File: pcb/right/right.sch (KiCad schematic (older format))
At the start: 103 parts, among them SW1 SW_Push, SW10 SW_Push, SW11 SW_Push, SW12 SW_Push, SW13 SW_Push, SW14 SW_Push, SW15 SW_Push, SW16 SW_Push, SW17 SW_Push, SW18 SW_Push, SW19 SW_Push, SW2 SW_Push, SW20 SW_Push, SW21 SW_Push, SW22 SW_Push, SW23 SW_Push, SW24 SW_Push, SW25 SW_Push, SW26 SW_Push, SW27 SW_Push, SW28 SW_Push, SW29 SW_Push, SW3 SW_Push, SW30 SW_Push, SW31 SW_Push, SW32 SW_Push, SW33 SW_Push, SW34 SW_Push, SW35 SW_Push, SW36 SW_Push, SW37 SW_Push, SW38 SW_Push, SW39 SW_Push, SW4 SW_Push, SW40 SW_Push, SW41 SW_Push, SW42 SW_Push, SW43 SW_Push, SW44 SW_Push, SW45 SW_Push, SW46 SW_Push, SW47 SW_Push, SW48 SW_Push, SW49 SW_Push, SW5 SW_Push, SW50 SW_Push, SW51 SW_Push, SW52 SW_Push, SW6 SW_Push, SW7 SW_Push, SW8 SW_Push, SW9 SW_Push

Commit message: pcb: Right key layout
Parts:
- SW43: footprint Button_Switch_Keyboard:SW_Cherry_MX_1.00u_PCB -> Button_Switch_Keyboard:SW_Cherry_MX_1.50u_PCB
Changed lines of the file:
@@
 F 0 "SW43" H 9950 2635 50  0000 C CNN
 F 1 "SW_Push" H 9950 2544 50  0000 C CNN
-F 2 "Button_Switch_Keyboard:SW_Cherry_MX_1.00u_PCB" H 9950 2550 50  0001 C CNN
+F 2 "Button_Switch_Keyboard:SW_Cherry_MX_1.50u_PCB" H 9950 2550 50  0001 C CNN
 F 3 "~" H 9950 2550 50  0001 C CNN
 	1    9950 2350

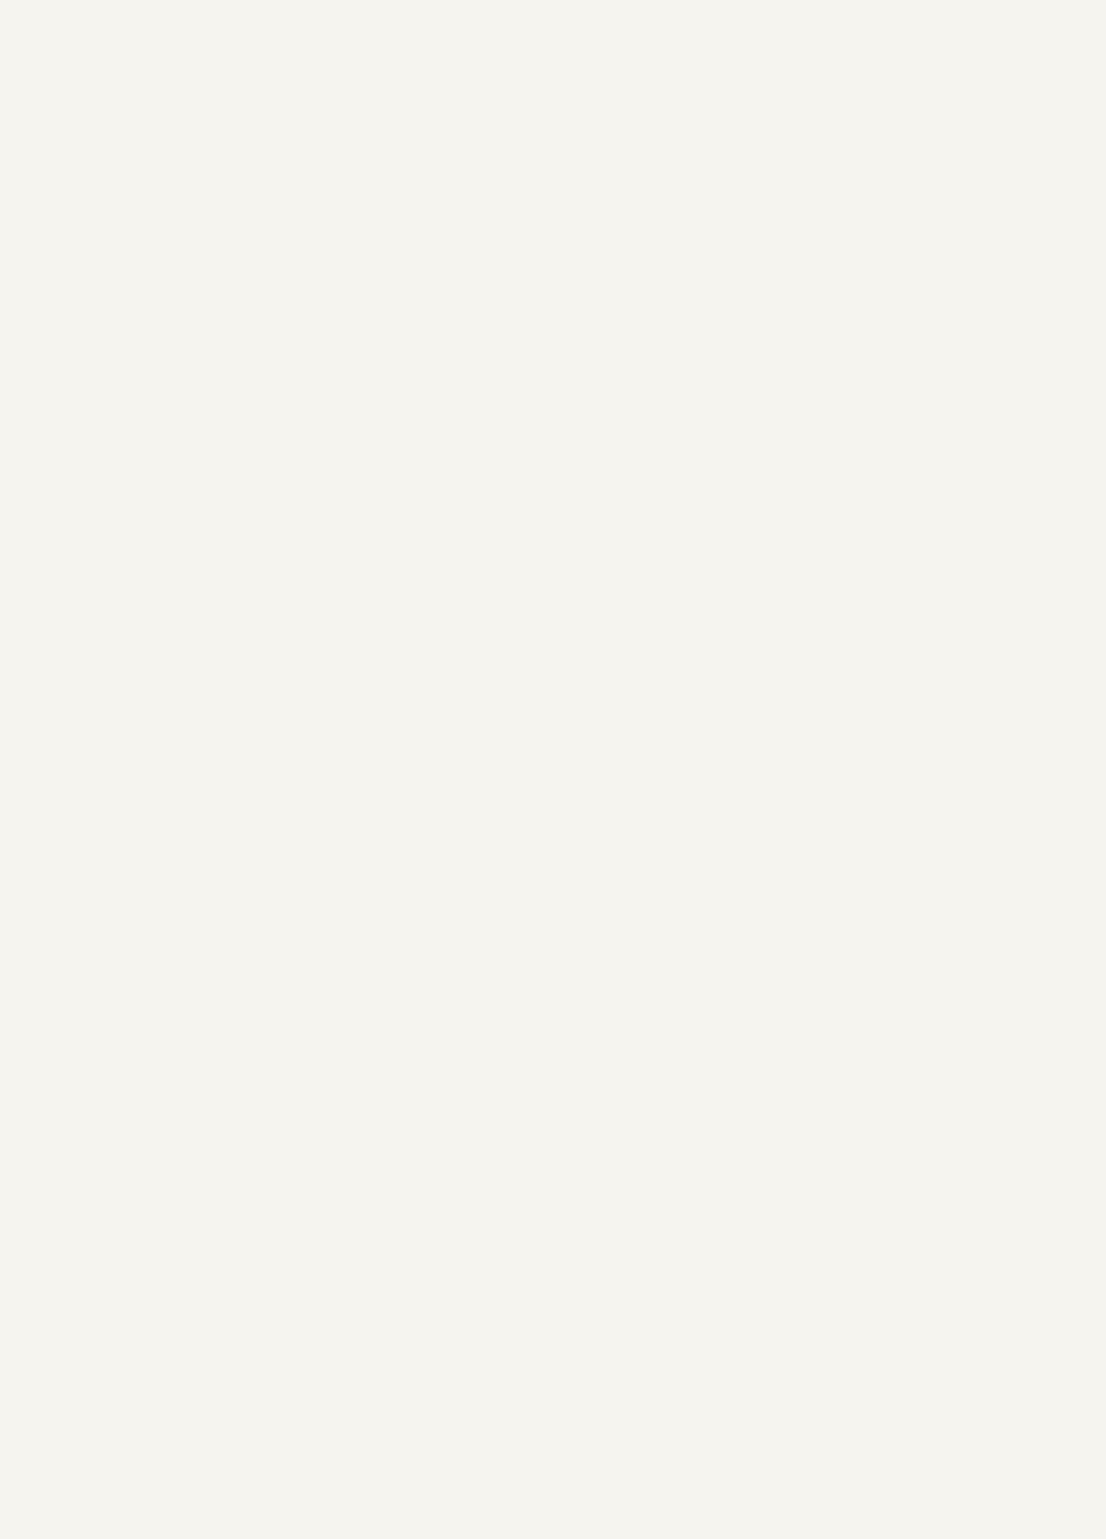
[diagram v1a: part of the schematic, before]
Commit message: pcb: right: Power to MCU
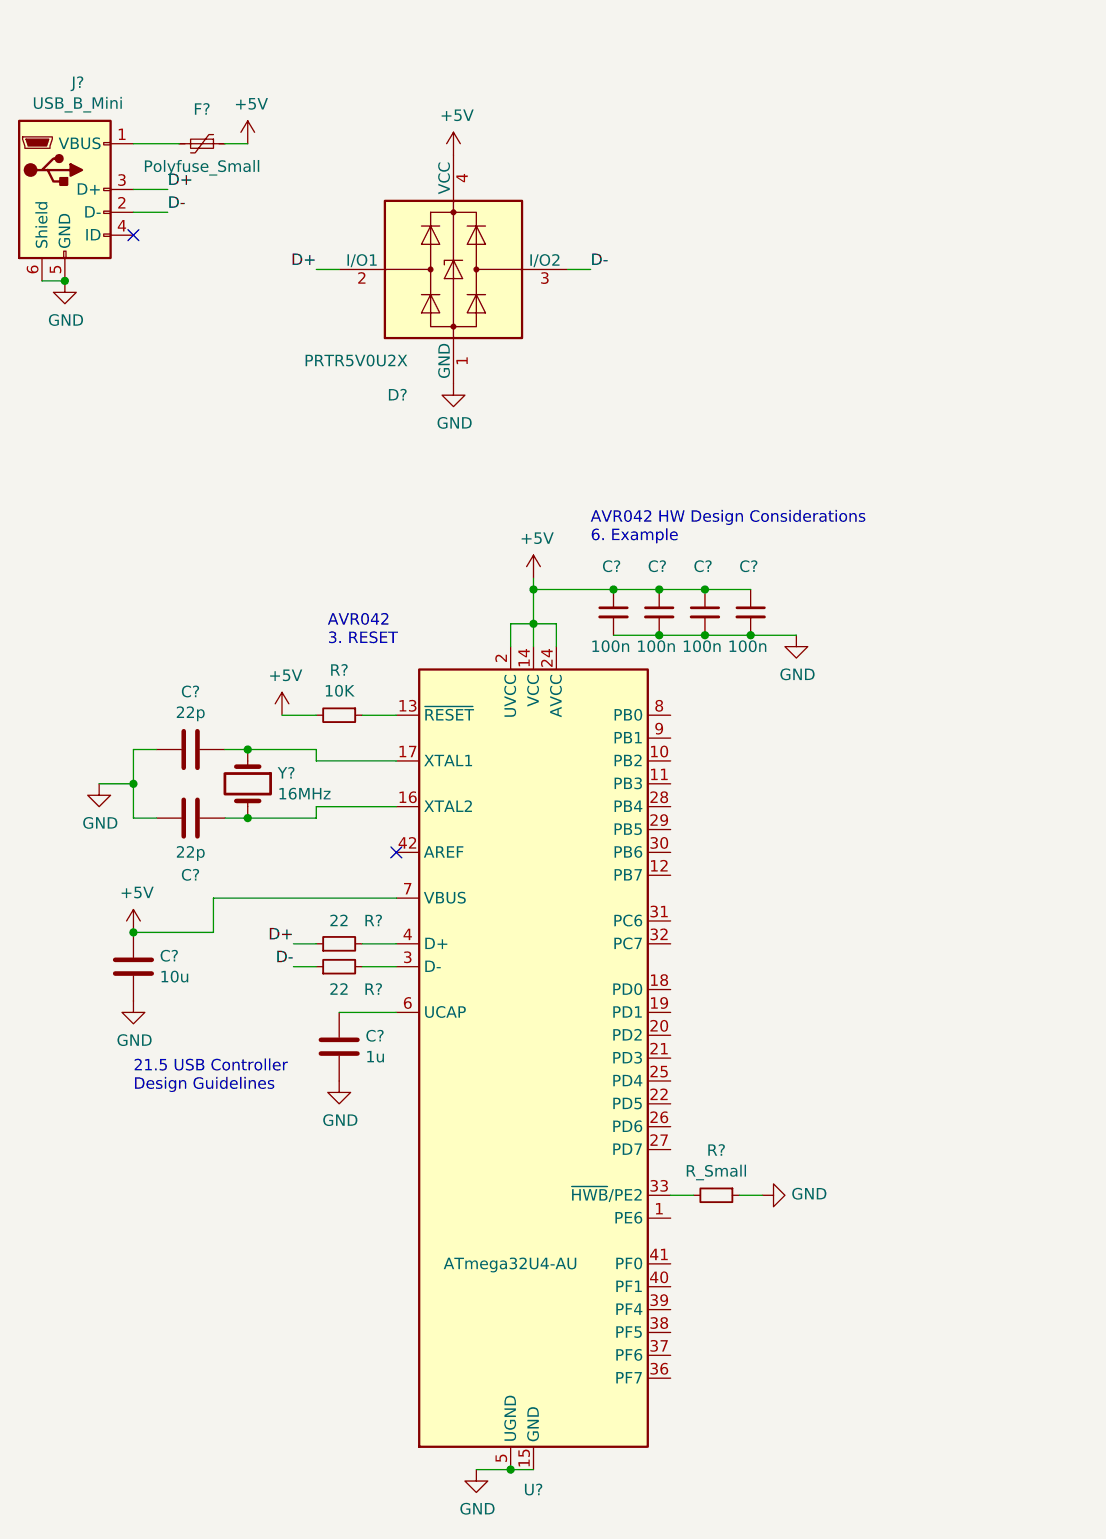
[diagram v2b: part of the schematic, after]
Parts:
- added C?: 1u, symbol Device:C
- added C? (x2): 22p, symbol Device:C
- added C?: 10u, symbol Device:C
- added C? (x4): 100n, symbol Device:C_Small
- added D?: PRTR5V0U2X, Package_TO_SOT_SMD:SOT-143, symbol Power_Protection:PRTR5V0U2X
- added F?: Polyfuse_Small, symbol Device:Polyfuse_Small
- added J?: USB_B_Mini, symbol Connector:USB_B_Mini
- added R?: R_Small, symbol Device:R_Small
- added R? (x2): 22, symbol Device:R_Small
- added R?: 10K, symbol Device:R_Small
- added U?: ATmega32U4-AU, Package_QFP:TQFP-44_10x10mm_P0.8mm, symbol MCU_Microchip_ATmega:ATmega32U4-AU
- added Y?: 16MHz, symbol Device:Crystal
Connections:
- net labels added: +5V, D+, D-, GND
- wire segments 120 -> 169
- no-connect marks 0 -> 2
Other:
- note added: "21.5 USB Controller\nDesign Guidelines"
- note added: "AVR042 HW Design Considerations\n6. Example"
- note added: "AVR042\n3. RESET"

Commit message: pcb: Right: Reset
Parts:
- added D?: D_Small, symbol Device:D_Small
- added SW?: SW_Push, symbol Switch:SW_Push
- R?: value R_Small -> 10K
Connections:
- wire segments 169 -> 175
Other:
- note added: "AVR042\n3. RESET\n+ Arduino"
- note removed: "AVR042\n3. RESET"
- moved on the sheet: R?
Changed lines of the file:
@@
 L power:+5V #PWR?
 U 1 1 604E6BA1
-P 1750 3700
-F 0 "#PWR?" H 1750 3550 50  0001 C CNN
-F 1 "+5V" H 1765 3873 50  0000 C CNN
-F 2 "" H 1750 3700 50  0001 C CNN
-F 3 "" H 1750 3700 50  0001 C CNN
-	1    1750 3700
+P 2150 3150
+F 0 "#PWR?" H 2150 3000 50  0001 C CNN
+F 1 "+5V" H 2165 3323 50  0000 C CNN
+F 2 "" H 2150 3150 50  0001 C CNN
+F 3 "" H 2150 3150 50  0001 C CNN
+	1    2150 3150
 	1    0    0    -1
 $EndComp
@@
 L Device:R_Small R?
 U 1 1 605D1F9D
-P 2000 3700
-F 0 "R?" V 1804 3700 50  0000 C CNN
-F 1 "10K" V 1895 3700 50  0000 C CNN
-F 2 "" H 2000 3700 50  0001 C CNN
-F 3 "~" H 2000 3700 50  0001 C CNN
-	1    2000 3700
-	0    1    1    0
-$EndComp
-Wire Wire Line
-	2100 3700 2250 3700
-Wire Wire Line
-	1900 3700 1750 3700
+P 2150 3300
+F 0 "R?" H 2050 3250 50  0000 C CNN
+F 1 "10K" H 2050 3350 50  0000 C CNN
+F 2 "" H 2150 3300 50  0001 C CNN
+F 3 "~" H 2150 3300 50  0001 C CNN
+	1    2150 3300
+	-1   0    0    1
+$EndComp
 $Comp
 L Device:C C?
@@
 Text Notes 3100 2950 0    50   ~ 0
 AVR042 HW Design Considerations\n6. Example
-Text Notes 1950 3400 0    50   ~ 0
-AVR042\n3. RESET
+Text Notes 1650 3100 0    50   ~ 0
+AVR042\n3. RESET\n+ Arduino
 $Comp
 L power:GND #PWR?
@@
 P 3650 5800
 F 0 "R?" V 3454 5800 50  0000 C CNN
-F 1 "R_Small" V 3545 5800 50  0000 C CNN
+F 1 "10K" V 3545 5800 50  0000 C CNN
 F 2 "" H 3650 5800 50  0001 C CNN
 F 3 "~" H 3650 5800 50  0001 C CNN
@@
 Wire Wire Line
 	3750 5800 3850 5800
+$Comp
+L Switch:SW_Push SW?
+U 1 1 60403708
+P 1900 3500
+F 0 "SW?" H 1900 3785 50  0000 C CNN
+F 1 "SW_Push" H 1900 3694 50  0000 C CNN
+F 2 "" H 1900 3700 50  0001 C CNN
+F 3 "~" H 1900 3700 50  0001 C CNN
+	1    1900 3500
+	1    0    0    -1
+$EndComp
+$Comp
+L power:GND #PWR?
+U 1 1 6040463B
+P 1600 3500
+F 0 "#PWR?" H 1600 3250 50  0001 C CNN
+F 1 "GND" H 1605 3327 50  0000 C CNN
+F 2 "" H 1600 3500 50  0001 C CNN
+F 3 "" H 1600 3500 50  0001 C CNN
+	1    1600 3500
+	1    0    0    -1
+$EndComp
+Wire Wire Line
+	1700 3500 1600 3500
+Wire Wire Line
+	2150 3150 2150 3200
+Wire Wire Line
+	2100 3500 2150 3500
+Wire Wire Line
+	2150 3500 2150 3700
+Wire Wire Line
+	2150 3700 2250 3700
+Wire Wire Line
+	2150 3400 2150 3500
+Connection ~ 2150 3500
+$Comp
+L Device:D_Small D?
+U 1 1 604C1548
+P 2400 3300
+F 0 "D?" V 2400 3370 50  0000 L CNN
+F 1 "D_Small" V 2445 3370 50  0001 L CNN
+F 2 "" V 2400 3300 50  0001 C CNN
+F 3 "~" V 2400 3300 50  0001 C CNN
+	1    2400 3300
+	0    1    1    0
+$EndComp
+Wire Wire Line
+	2400 3400 2150 3400
+Connection ~ 2150 3400
+Wire Wire Line
+	2400 3200 2150 3200
+Connection ~ 2150 3200
 $EndSCHEMATC

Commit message: pcb: right: ICSP, I2C
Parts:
- added C?: 100n, symbol Device:C_Small
- added J?: ICSP, symbol Connector_Generic:Conn_02x03_Odd_Even
- added J?: To Left Part, symbol Connector_Generic:Conn_02x02_Odd_Even
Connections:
- net labels added: MISO, MOSI, RESET, SCK, SCL, SDA
- wire segments 175 -> 192
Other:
- moved on the sheet: D?, F?, J?, R?, SW?

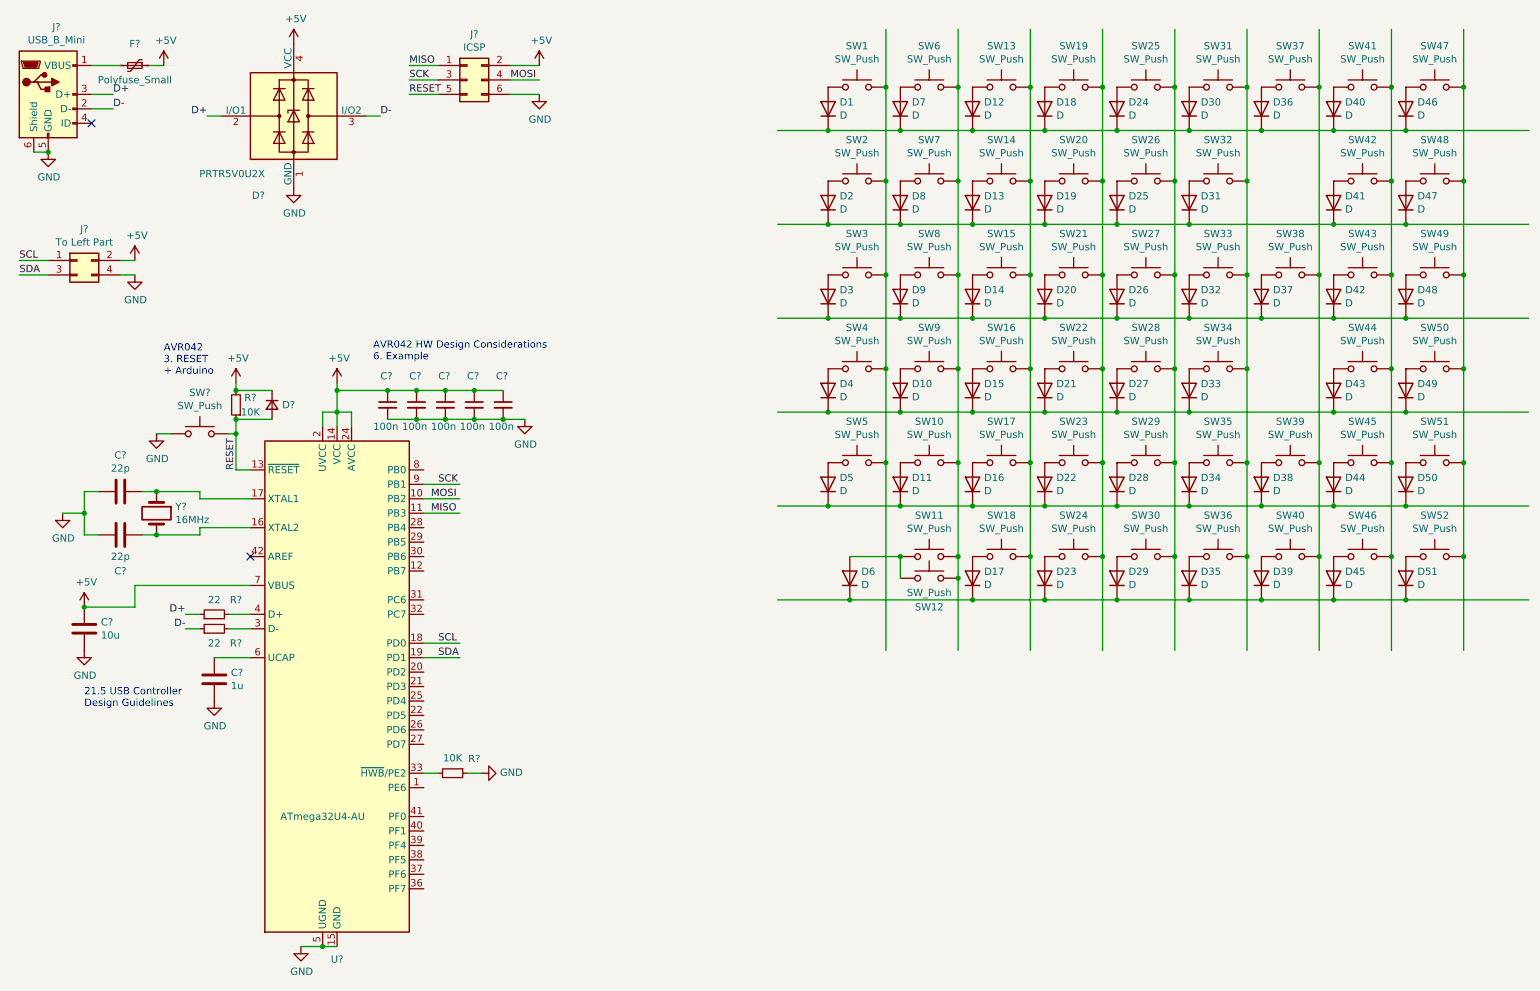
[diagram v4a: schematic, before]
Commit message: pcb: right: Finish schematics
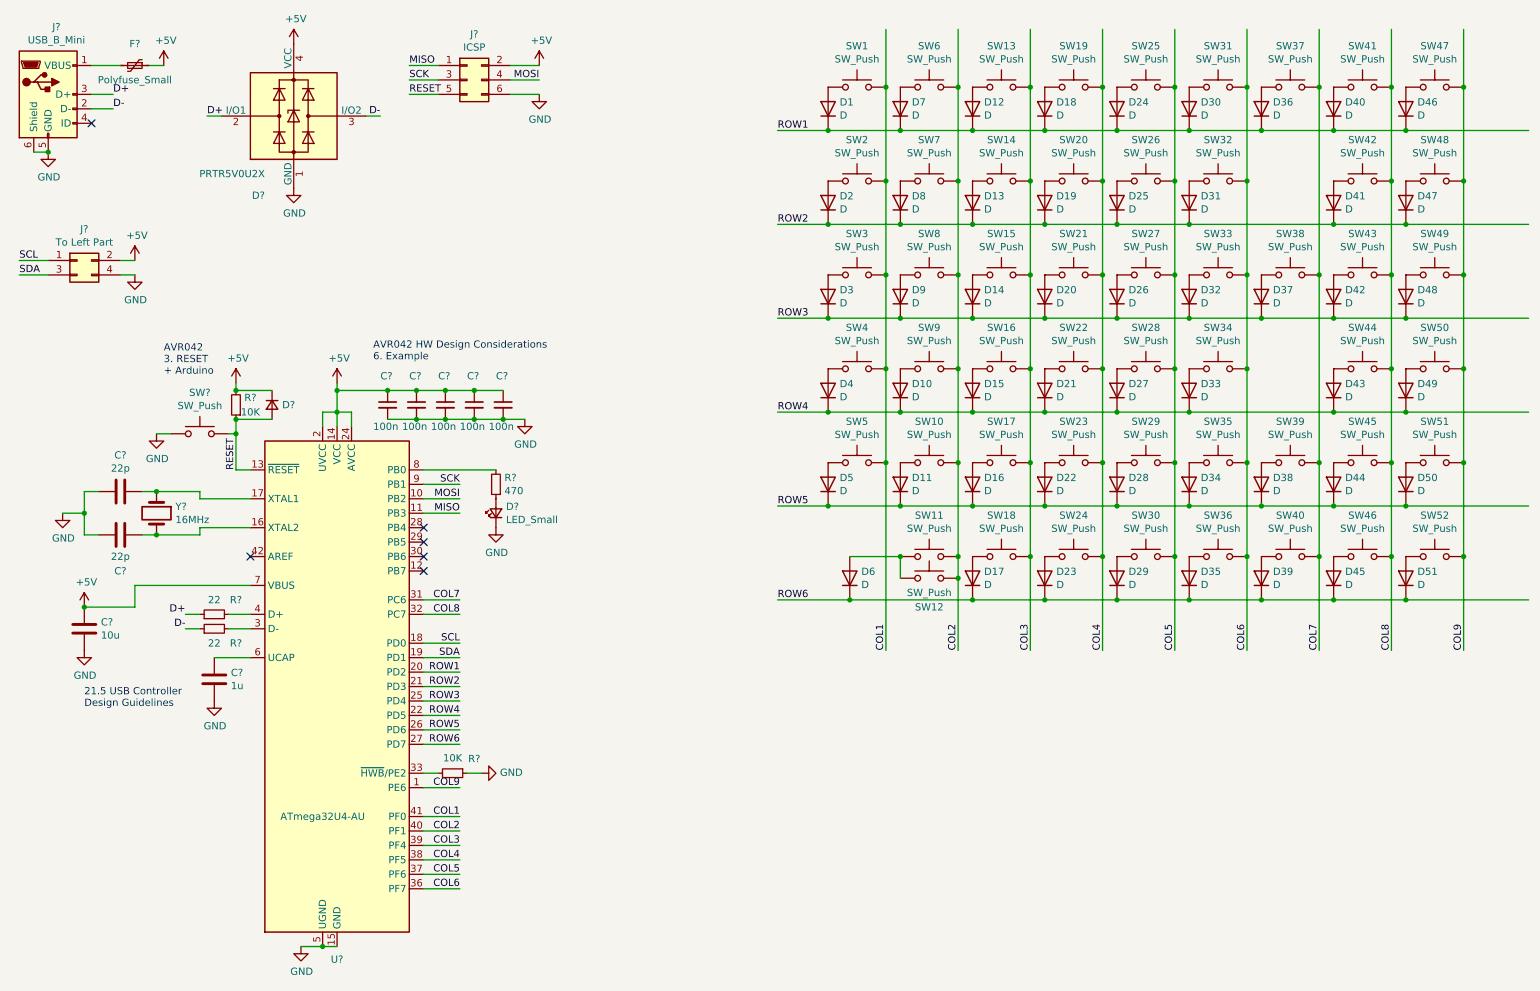
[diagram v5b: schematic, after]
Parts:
- added D?: LED_Small, symbol Device:LED_Small
- added R?: 470, symbol Device:R_Small
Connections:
- net labels added: COL1, COL2, COL3, COL4, COL5, COL6, COL7, COL8, COL9, ROW1, ROW2, ROW3, ROW4, ROW5, ROW6
- wire segments 192 -> 208
- no-connect marks 2 -> 6
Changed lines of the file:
@@
 Wire Wire Line
 	6250 3300 6750 3300
-Wire Wire Line
-	5900 3950 6250 3950
 $Comp
 L Switch:SW_Push SW5
@@
 	0    -1   -1   0
 $EndComp
-Connection ~ 6250 3950
 Wire Wire Line
 	6250 3950 6750 3950
@@
 Text Label 1300 1200 0    50   ~ 0
 D-
-Text Label 1950 1250 2    50   ~ 0
+Text Label 1950 1250 0    50   ~ 0
 D+
-Text Label 3150 1250 0    50   ~ 0
+Text Label 3150 1250 2    50   ~ 0
 D-
 Wire Wire Line
@@
 Text Label 3350 900  0    50   ~ 0
 MISO
-Text Label 4050 1000 0    50   ~ 0
+Text Label 4250 1000 2    50   ~ 0
 MOSI
 $Comp
@@
 Wire Wire Line
 	3450 3900 3700 3900
-Text Label 3500 3900 0    50   ~ 0
+Text Label 3700 3900 2    50   ~ 0
 MOSI
-Text Label 3500 4000 0    50   ~ 0
+Text Label 3700 4000 2    50   ~ 0
 MISO
-Text Label 3550 3800 0    50   ~ 0
+Text Label 3700 3800 2    50   ~ 0
 SCK
 Wire Wire Line
@@
 Wire Wire Line
 	3450 3800 3700 3800
-Text Label 3550 4900 0    50   ~ 0
+Text Label 3700 4900 2    50   ~ 0
 SCL
-Text Label 3550 5000 0    50   ~ 0
+Text Label 3700 5000 2    50   ~ 0
 SDA
 Wire Wire Line
@@
 	3800 3150 4000 3150
 Connection ~ 3800 3150
+Text Label 5900 1350 0    50   ~ 0
+ROW1
+Text Label 5900 2000 0    50   ~ 0
+ROW2
+Text Label 5900 2650 0    50   ~ 0
+ROW3
+Text Label 5900 3300 0    50   ~ 0
+ROW4
+Text Label 5900 3950 0    50   ~ 0
+ROW5
+Text Label 5900 4600 0    50   ~ 0
+ROW6
+Text Label 6650 4950 1    50   ~ 0
+COL1
+Text Label 7150 4950 1    50   ~ 0
+COL2
+Text Label 7650 4950 1    50   ~ 0
+COL3
+Text Label 8150 4950 1    50   ~ 0
+COL4
+Text Label 8650 4950 1    50   ~ 0
+COL5
+Text Label 9150 4950 1    50   ~ 0
+COL6
+Text Label 9650 4950 1    50   ~ 0
+COL7
+Text Label 10150 4950 1    50   ~ 0
+COL8
+Text Label 10650 4950 1    50   ~ 0
+COL9
+Text Label 3700 5100 2    50   ~ 0
+ROW1
+Text Label 3700 5200 2    50   ~ 0
+ROW2
+Text Label 3700 5300 2    50   ~ 0
+ROW3
+Text Label 3700 5400 2    50   ~ 0
+ROW4
+Text Label 3700 5500 2    50   ~ 0
+ROW5
+Text Label 3700 5600 2    50   ~ 0
+ROW6
+Wire Wire Line
+	3700 5100 3450 5100
+Wire Wire Line
+	3700 5200 3450 5200
+Wire Wire Line
+	3700 5300 3450 5300
+Wire Wire Line
+	3700 5400 3450 5400
+Wire Wire Line
+	3700 5500 3450 5500
+Wire Wire Line
+	3700 5600 3450 5600
+Text Label 3700 6100 2    50   ~ 0
+COL1
+Text Label 3700 6200 2    50   ~ 0
+COL2
+Text Label 3700 6300 2    50   ~ 0
+COL3
+Text Label 3700 6400 2    50   ~ 0
+COL4
+Text Label 3700 6500 2    50   ~ 0
+COL5
+Text Label 3700 6600 2    50   ~ 0
+COL6
+Text Label 3700 4600 2    50   ~ 0
+COL7
+Text Label 3700 4700 2    50   ~ 0
+COL8
+Text Label 3700 5900 2    50   ~ 0
+COL9
+Wire Wire Line
+	3450 6100 3700 6100
+Wire Wire Line
+	3450 6200 3700 6200
+Wire Wire Line
+	3450 6300 3700 6300
+Wire Wire Line
+	3450 6400 3700 6400
+Wire Wire Line
+	3450 6500 3700 6500
+Wire Wire Line
+	3700 6600 3450 6600
+Wire Wire Line
+	3700 4700 3450 4700
+Wire Wire Line
+	3700 5900 3450 5900
+Connection ~ 6250 3950
+Wire Wire Line
+	3700 4600 3450 4600
+Wire Wire Line
+	5900 3950 6250 3950
+$Comp
+L Device:R_Small R?
+U 1 1 60FD0E07
+P 3950 3800
+F 0 "R?" H 3891 3754 50  0000 R CNN
+F 1 "470" H 3891 3845 50  0000 R CNN
+F 2 "" H 3950 3800 50  0001 C CNN
+F 3 "~" H 3950 3800 50  0001 C CNN
+	1    3950 3800
+	-1   0    0    1
+$EndComp
+$Comp
+L Device:LED_Small D?
+U 1 1 60FF28A8
+P 3950 4000
+F 0 "D?" V 3996 3930 50  0000 R CNN
+F 1 "LED_Small" V 3905 3930 50  0000 R CNN
+F 2 "" V 3950 4000 50  0001 C CNN
+F 3 "~" V 3950 4000 50  0001 C CNN
+	1    3950 4000
+	0    -1   -1   0
+$EndComp
+$Comp
+L power:GND #PWR?
+U 1 1 60FF4D85
+P 3950 4100
+F 0 "#PWR?" H 3950 3850 50  0001 C CNN
+F 1 "GND" H 3955 3927 50  0000 C CNN
+F 2 "" H 3950 4100 50  0001 C CNN
+F 3 "" H 3950 4100 50  0001 C CNN
+	1    3950 4100
+	1    0    0    -1
+$EndComp
+Wire Wire Line
+	3450 3700 3950 3700
+NoConn ~ 3450 4100
+NoConn ~ 3450 4200
+NoConn ~ 3450 4300
+NoConn ~ 3450 4400
 $EndSCHEMATC
